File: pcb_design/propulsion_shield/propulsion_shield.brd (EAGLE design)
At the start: 100 x 56 mm, 62 parts

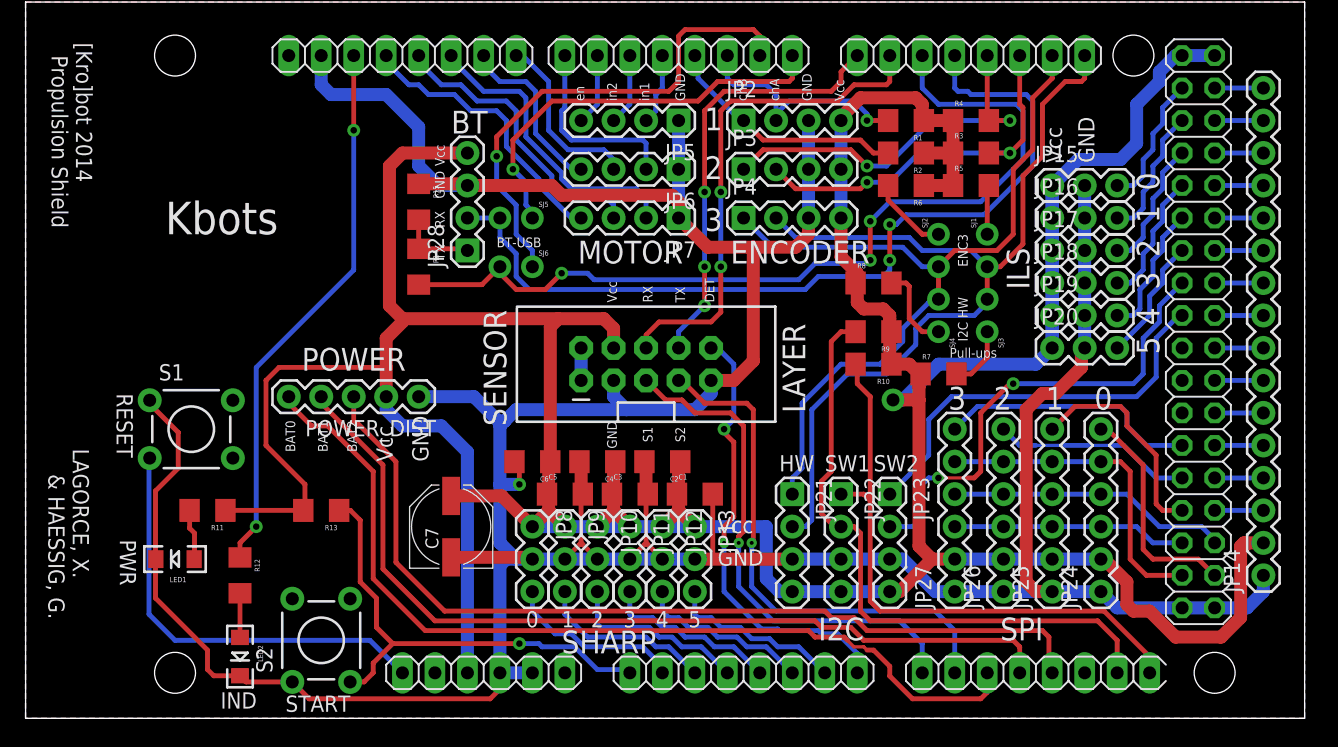
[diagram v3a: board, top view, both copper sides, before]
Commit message: [propulsion_shield] Added a buzzer on the board
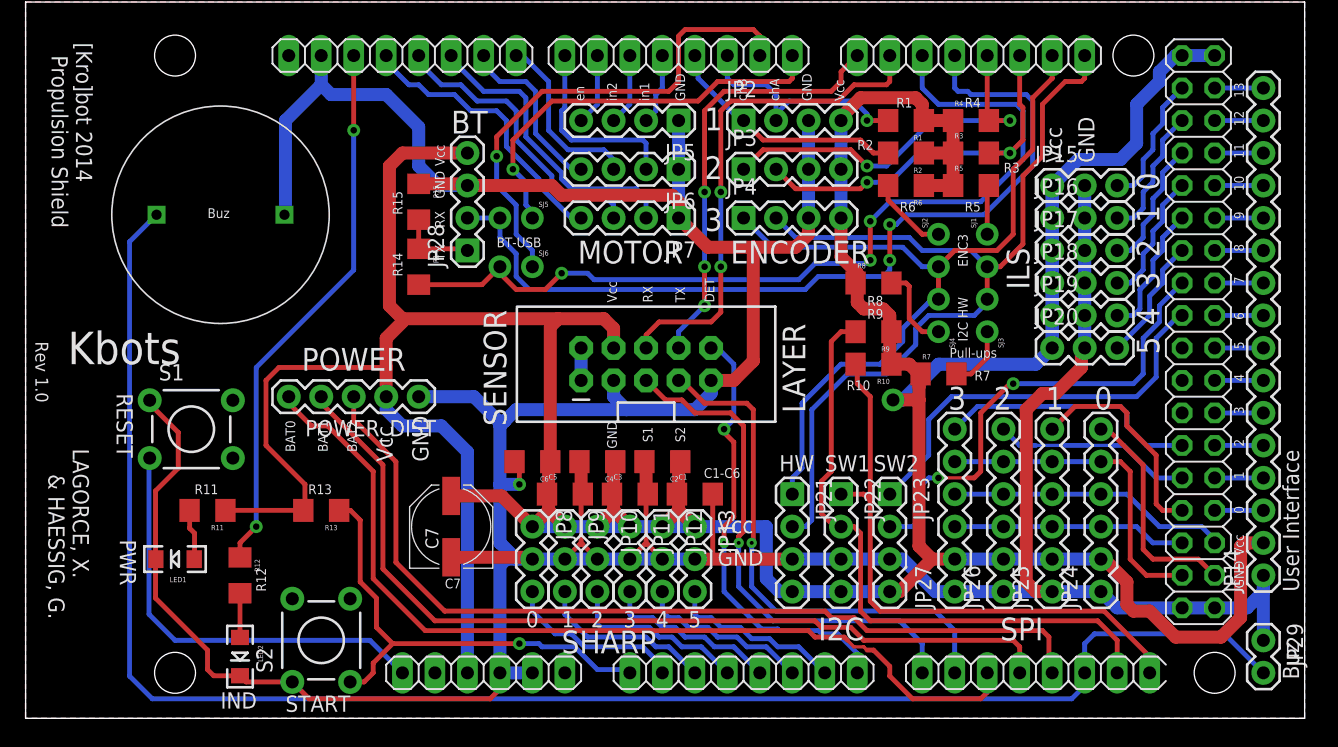
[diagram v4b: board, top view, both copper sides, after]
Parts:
- added JP29: M02PTH, SparkFun-Connectors:1X02
- added U$1: BUZZER, buzzerG:BUZZER
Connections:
- new net BUZZER: IC1.20, JP29.2, U$1.P$1
- net GND: now also JP29.1, U$1.P$2
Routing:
- net BUZZER: track 0.00 -> 131.6 mm
- net GND: track 323.7 -> 340.1 mm
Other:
- board text added: "10"
- board text added: "11"
- board text added: "12"
- board text added: "13"
- board text added: "6"
- board text added: "7"
- board text added: "8"
- board text added: "9"
- board text added: "Buz"
- board text added: "C1-C6"
- board text added: "C7"
- board text added: "R1"
- board text added: "R10"
- board text added: "R11"
- board text added: "R12"
- board text added: "R13"
- board text added: "R14"
- board text added: "R15"
- board text added: "R2"
- board text added: "R3"
- board text added: "R4"
- board text added: "R5"
- board text added: "R6"
- board text added: "R7"
- board text added: "R8"
- board text added: "R9"
- board text added: "Rev 1.0"
- board text added: "User Interface"
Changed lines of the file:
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@@
 <layer number="23" name="tOrigins" color="15" fill="1" visible="yes" active="yes"/>
 <layer number="24" name="bOrigins" color="15" fill="1" visible="yes" active="yes"/>
-<layer number="25" name="tNames" color="7" fill="1" visible="yes" active="yes"/>
+<layer number="25" name="tNames" color="7" fill="1" visible="no" active="yes"/>
 <layer number="26" name="bNames" color="7" fill="1" visible="no" active="yes"/>
 <layer number="27" name="tValues" color="7" fill="1" visible="no" active="yes"/>
@@
 <text x="2.032" y="52.832" size="1.27" layer="21" font="vector" ratio="15" rot="SR270">[Kro]bot 2014
   Propulsion Shield</text>
-<text x="10.922" y="37.846" size="2.54" layer="21" font="vector" ratio="15" rot="SR0">Kbots</text>
+<text x="3.302" y="27.686" size="2.54" layer="21" font="vector" ratio="15" rot="SR0">Kbots</text>
 <text x="46.228" y="32.512" size="0.762" layer="21" font="vector" ratio="15" rot="R90">Vcc</text>
 <text x="46.228" y="21.082" size="0.762" layer="21" font="vector" ratio="15" rot="R90">GND</text>
@@
 <text x="49.022" y="21.59" size="0.762" layer="21" font="vector" ratio="15" rot="R90">S1</text>
 <text x="51.562" y="21.59" size="0.762" layer="21" font="vector" ratio="15" rot="R90">S2</text>
+<text x="13.208" y="17.526" size="0.762" layer="21" font="vector" ratio="15">R11</text>
+<text x="22.098" y="17.526" size="0.762" layer="21" font="vector" ratio="15">R13</text>
+<text x="18.796" y="9.906" size="0.762" layer="21" font="vector" ratio="15" rot="R90">R12</text>
+<text x="34.036" y="10.922" size="0.762" layer="21" font="vector" ratio="15" rot="R180">C7</text>
+<text x="55.88" y="19.558" size="0.762" layer="21" font="vector" ratio="15" rot="R180">C1-C6</text>
+<text x="75.438" y="27.178" size="0.762" layer="21" font="vector" ratio="15" rot="R180">R7</text>
+<text x="66.04" y="26.416" size="0.762" layer="21" font="vector" ratio="15" rot="R180">R10</text>
+<text x="67.056" y="32.004" size="0.762" layer="21" font="vector" ratio="15" rot="R180">R9</text>
+<text x="67.056" y="33.02" size="0.762" layer="21" font="vector" ratio="15" rot="R180">R8</text>
+<text x="69.596" y="40.386" size="0.762" layer="21" font="vector" ratio="15" rot="R180">R6</text>
+<text x="74.676" y="40.386" size="0.762" layer="21" font="vector" ratio="15" rot="R180">R5</text>
+<text x="77.724" y="43.434" size="0.762" layer="21" font="vector" ratio="15" rot="R180">R3</text>
+<text x="74.676" y="48.514" size="0.762" layer="21" font="vector" ratio="15" rot="R180">R4</text>
+<text x="68.072" y="47.752" size="0.762" layer="21" font="vector" ratio="15">R1</text>
+<text x="65.024" y="44.45" size="0.762" layer="21" font="vector" ratio="15">R2</text>
+<text x="29.464" y="34.544" size="0.762" layer="21" font="vector" ratio="15" rot="R90">R14</text>
+<text x="29.464" y="39.37" size="0.762" layer="21" font="vector" ratio="15" rot="R90">R15</text>
+<text x="14.224" y="39.116" size="0.762" layer="21" font="vector" ratio="15">Buz</text>
+<text x="99.568" y="3.048" size="1.27" layer="21" font="vector" ratio="15" rot="R90">Buz</text>
+<text x="99.568" y="9.906" size="1.27" layer="21" font="vector" ratio="15" rot="R90">User Interface</text>
+<text x="95.25" y="10.16" size="0.762" layer="21" font="vector" ratio="15" rot="R90">GND</text>
+<text x="95.25" y="12.7" size="0.762" layer="21" font="vector" ratio="15" rot="R90">Vcc</text>
+<text x="95.25" y="16.002" size="0.762" layer="21" font="vector" ratio="15" rot="R90">0</text>
+<text x="95.25" y="48.514" size="0.762" layer="21" font="vector" ratio="15" rot="R90">13</text>
+<text x="94.488" y="19.304" size="0.762" layer="21" font="vector" ratio="15" rot="R270">1</text>
+<text x="94.488" y="21.844" size="0.762" layer="21" font="vector" ratio="15" rot="R270">2</text>
+<text x="94.488" y="24.384" size="0.762" layer="21" font="vector" ratio="15" rot="R270">3</text>
+<text x="94.488" y="26.924" size="0.762" layer="21" font="vector" ratio="15" rot="R270">4</text>
+<text x="94.488" y="29.464" size="0.762" layer="21" font="vector" ratio="15" rot="R270">5</text>
+<text x="94.488" y="31.75" size="0.762" layer="21" font="vector" ratio="15" rot="R270">6</text>
+<text x="94.488" y="34.544" size="0.762" layer="21" font="vector" ratio="15" rot="R270">7</text>
+<text x="94.488" y="37.084" size="0.762" layer="21" font="vector" ratio="15" rot="R270">8</text>
+<text x="94.488" y="39.624" size="0.762" layer="21" font="vector" ratio="15" rot="R270">9</text>
+<text x="94.488" y="42.418" size="0.762" layer="21" font="vector" ratio="15" rot="R270">10</text>
+<text x="94.488" y="44.958" size="0.762" layer="21" font="vector" ratio="15" rot="R270">11</text>
+<text x="94.488" y="47.498" size="0.762" layer="21" font="vector" ratio="15" rot="R270">12</text>
+<text x="0.762" y="29.464" size="1.016" layer="21" font="vector" ratio="15" rot="SR270">Rev 1.0</text>
 </plain>
 <attributes>
@@
 <element name="SJ5" library="SparkFun-Passives" package="PTH-JUMPER-2-NO_NO_SILK" value="JUMPER-PTH-2-NO" x="38.354" y="39.116" rot="R180"/>
 <element name="SJ6" library="SparkFun-Passives" package="PTH-JUMPER-2-NO_NO_SILK" value="JUMPER-PTH-2-NO" x="38.354" y="35.306" rot="R180"/>
+<element name="U$1" library="buzzerG" package="BUZZER" value="BUZZER" x="15.24" y="39.37"/>
+<element name="JP29" library="SparkFun-Connectors" package="1X02" value="M02PTH" x="96.774" y="6.096" rot="R270"/>
 </elements>
 <signals>
@@
 <wire x1="34.544" y1="41.656" x2="34.414" y2="41.786" width="1.016" layer="1"/>
 <wire x1="34.414" y1="41.786" x2="30.734" y2="41.786" width="1.016" layer="1"/>
-<wire x1="23.114" y1="51.816" x2="23.114" y2="49.53" width="1.016" layer="16"/>
 <wire x1="23.114" y1="49.53" x2="23.876" y2="48.768" width="1.016" layer="16"/>
 <wire x1="23.876" y1="48.768" x2="28.194" y2="48.768" width="1.016" layer="16"/>
@@
 <vertex x="100" y="0"/>
 </polygon>
+<contactref element="U$1" pad="P$2"/>
+<contactref element="JP29" pad="1"/>
+<wire x1="96.774" y1="6.096" x2="96.774" y2="11.176" width="1.016" layer="16"/>
+<wire x1="23.114" y1="51.816" x2="23.114" y2="49.53" width="1.016" layer="16"/>
+<wire x1="23.114" y1="49.53" x2="20.32" y2="46.736" width="1.016" layer="16"/>
+<wire x1="20.32" y1="46.736" x2="20.32" y2="39.37" width="1.016" layer="16"/>
 </signal>
 <signal name="RESET">
@@
 <wire x1="25.4" y1="16.256" x2="24.514" y2="16.256" width="0.381" layer="1"/>
 </signal>
+<signal name="BUZZER">
+<contactref element="IC1" pad="20"/>
+<contactref element="JP29" pad="2"/>
+<contactref element="U$1" pad="P$1"/>
+<wire x1="96.774" y1="3.556" x2="93.726" y2="6.604" width="0.381" layer="16"/>
+<wire x1="93.726" y1="6.604" x2="83.566" y2="6.604" width="0.381" layer="16"/>
+<wire x1="83.566" y1="6.604" x2="82.804" y2="5.842" width="0.381" layer="16"/>
+<wire x1="82.804" y1="5.842" x2="82.804" y2="3.556" width="0.381" layer="16"/>
+<wire x1="82.804" y1="3.556" x2="82.804" y2="2.54" width="0.381" layer="16"/>
+<wire x1="82.804" y1="2.54" x2="81.788" y2="1.524" width="0.381" layer="16"/>
+<wire x1="81.788" y1="1.524" x2="9.906" y2="1.524" width="0.381" layer="16"/>
+<wire x1="9.906" y1="1.524" x2="8.128" y2="3.302" width="0.381" layer="16"/>
+<wire x1="8.128" y1="3.302" x2="8.128" y2="37.258" width="0.381" layer="16"/>
+<wire x1="8.128" y1="37.258" x2="10.24" y2="39.37" width="0.381" layer="16"/>
+</signal>
 </signals>

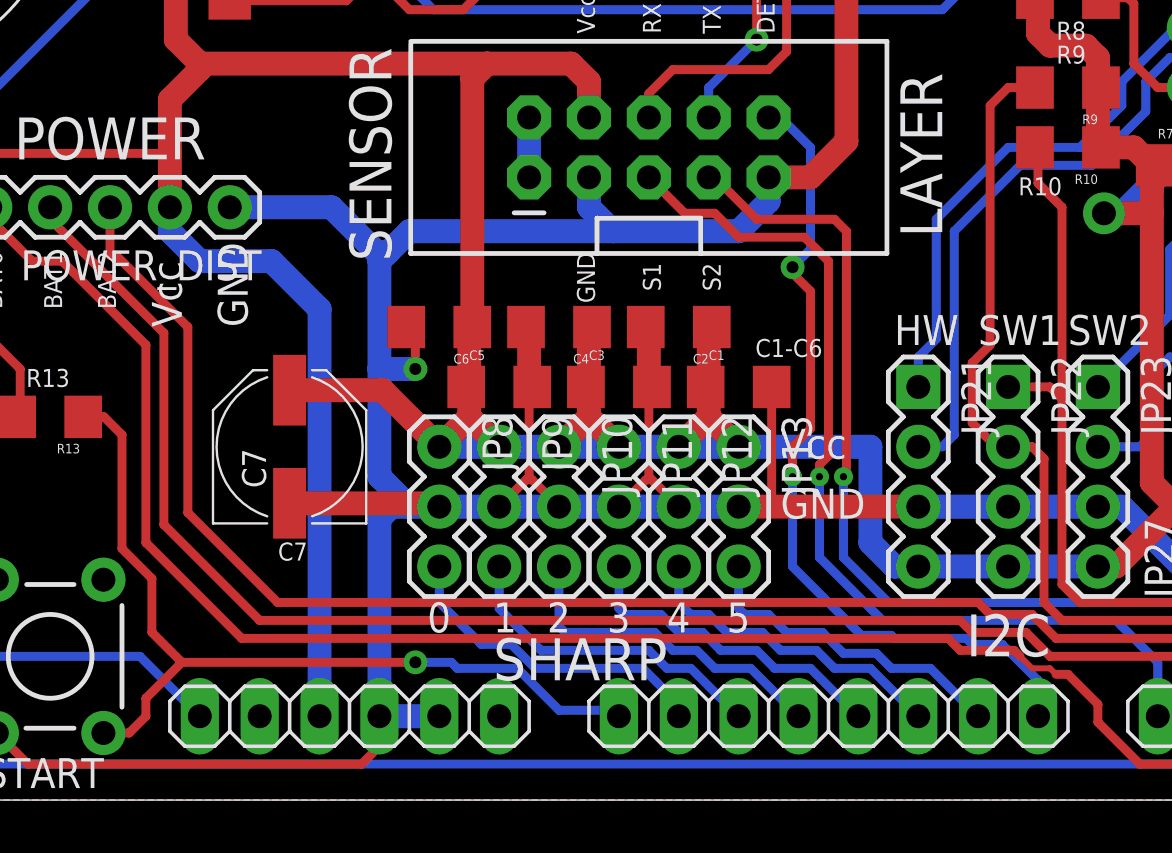
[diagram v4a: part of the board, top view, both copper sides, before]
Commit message: [PCB/propulsion_shield] Correction routing of power supply to Vin arduino pin (schematics + PCB)
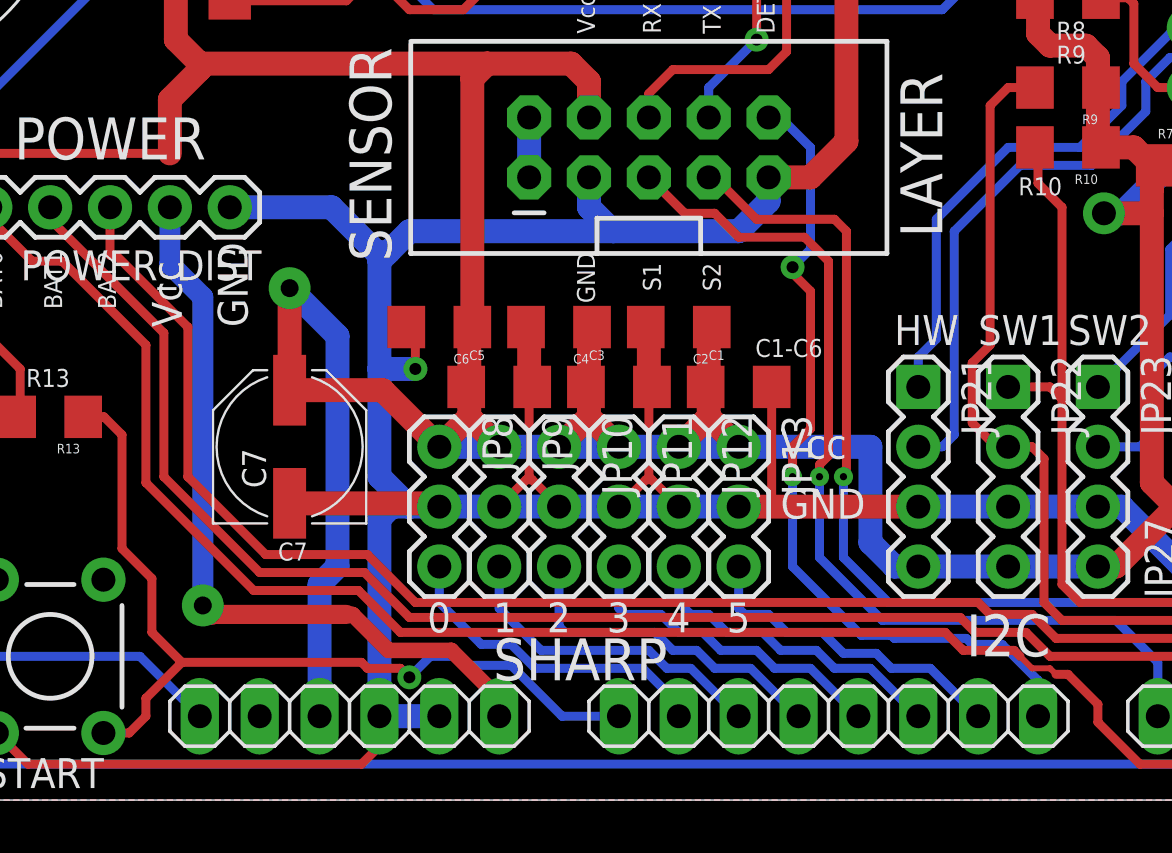
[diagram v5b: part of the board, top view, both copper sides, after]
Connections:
- removed net +VIN: IC1.6
- new net VDD: IC1.6, POWER_DIST.2
- net VCC: no longer POWER_DIST.2
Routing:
- net VDD: track 0.00 -> 32.4 mm, vias 0 -> 1
- net VCC: track 371.3 -> 366.6 mm, vias 1 -> 2
- net BAT_0: track 71.8 -> 70.3 mm
- net BAT_1: track 69.8 -> 68.6 mm
- net BAT_2: track 70.8 -> 70.0 mm
- net START_BTN: track 37.2 -> 37.9 mm
